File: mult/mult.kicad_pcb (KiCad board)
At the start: 2 copper layers, 76 parts, among them J1 Eurorack_Power, J10 Eurorack_Mono_Jack, J11 Eurorack_Mono_Jack, J12 Eurorack_Mono_Jack, J13 Eurorack_Mono_Jack, J14 Eurorack_Mono_Jack, J15 Eurorack_Mono_Jack, J16 Eurorack_Mono_Jack, J17 Eurorack_Mono_Jack, J2 Eurorack_Mono_Jack, J3 Eurorack_Mono_Jack, J4 Eurorack_Mono_Jack, J5 Eurorack_Mono_Jack, J6 Eurorack_Mono_Jack, J7 Eurorack_Mono_Jack, J8 Eurorack_Mono_Jack, J9 Eurorack_Mono_Jack, U1 OPA4197xPW, U2 OPA4197xPW, U3 OPA4197xPW, U4 OPA4197xPW, U5 LM324

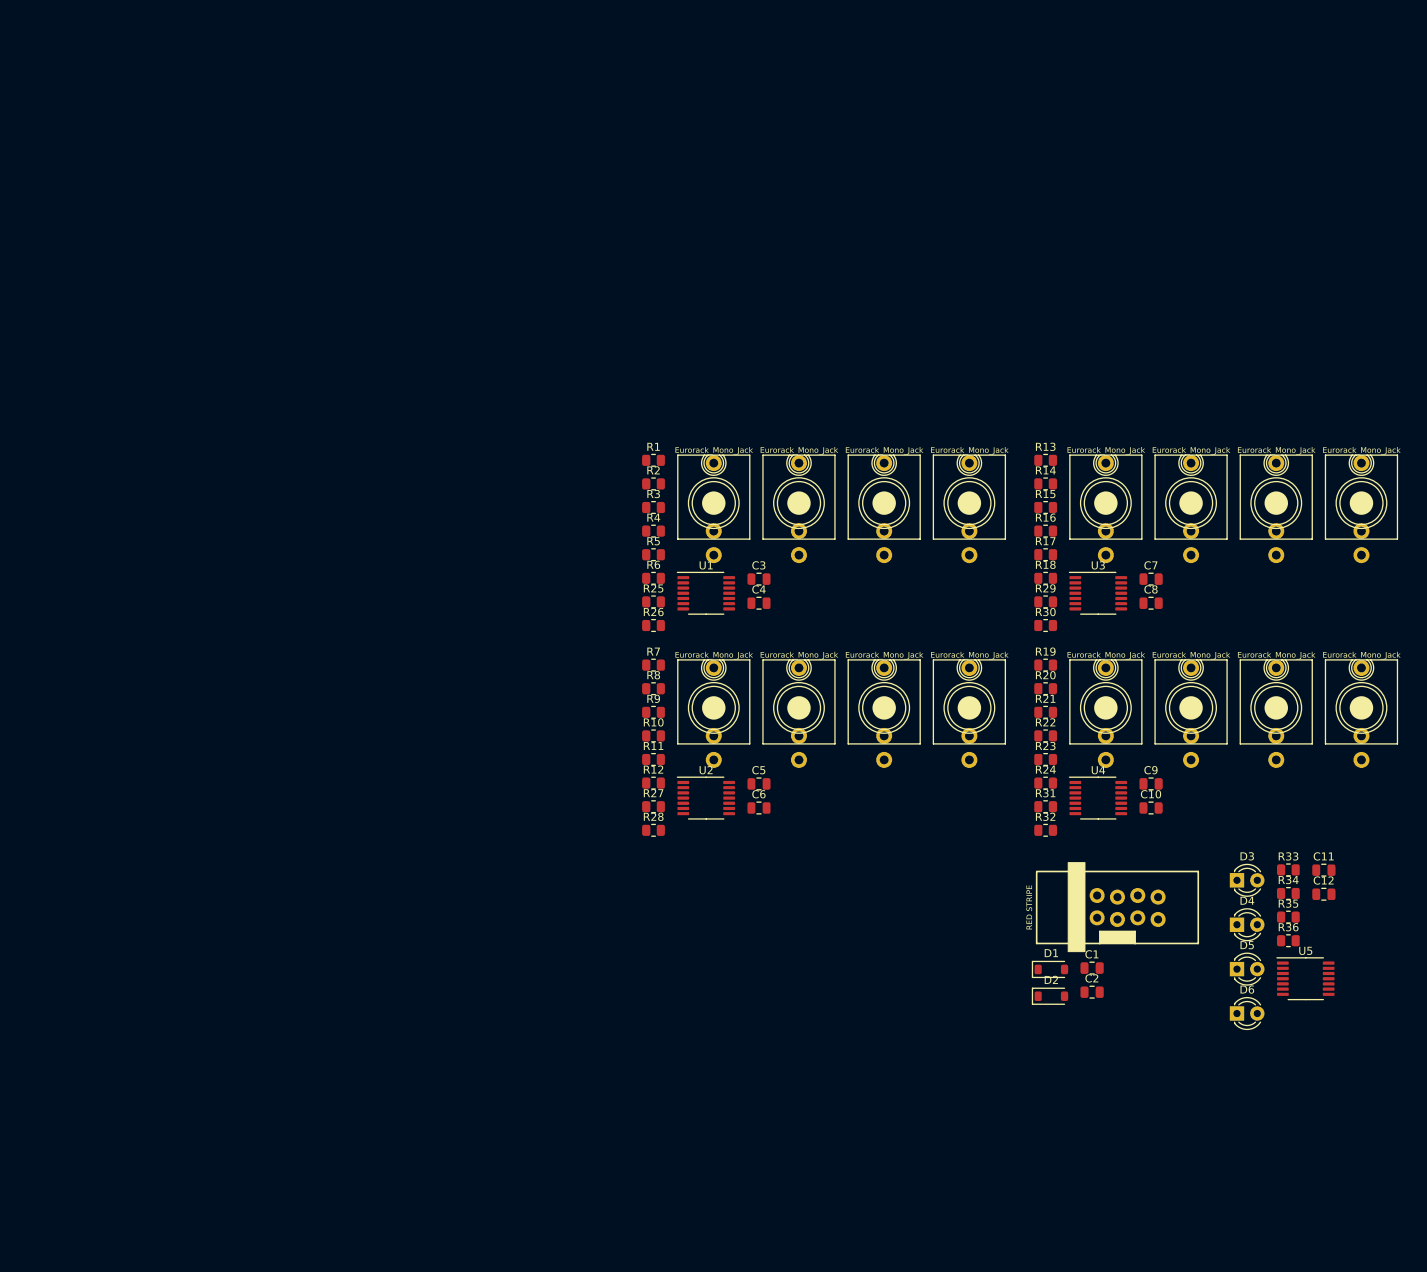
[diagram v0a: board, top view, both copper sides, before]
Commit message: mult: Misc partial progress
At least since last commit:

* New LEDs (no dual unit)
* Jack placement, share sleeve pin
* Board fit within 20x108mm
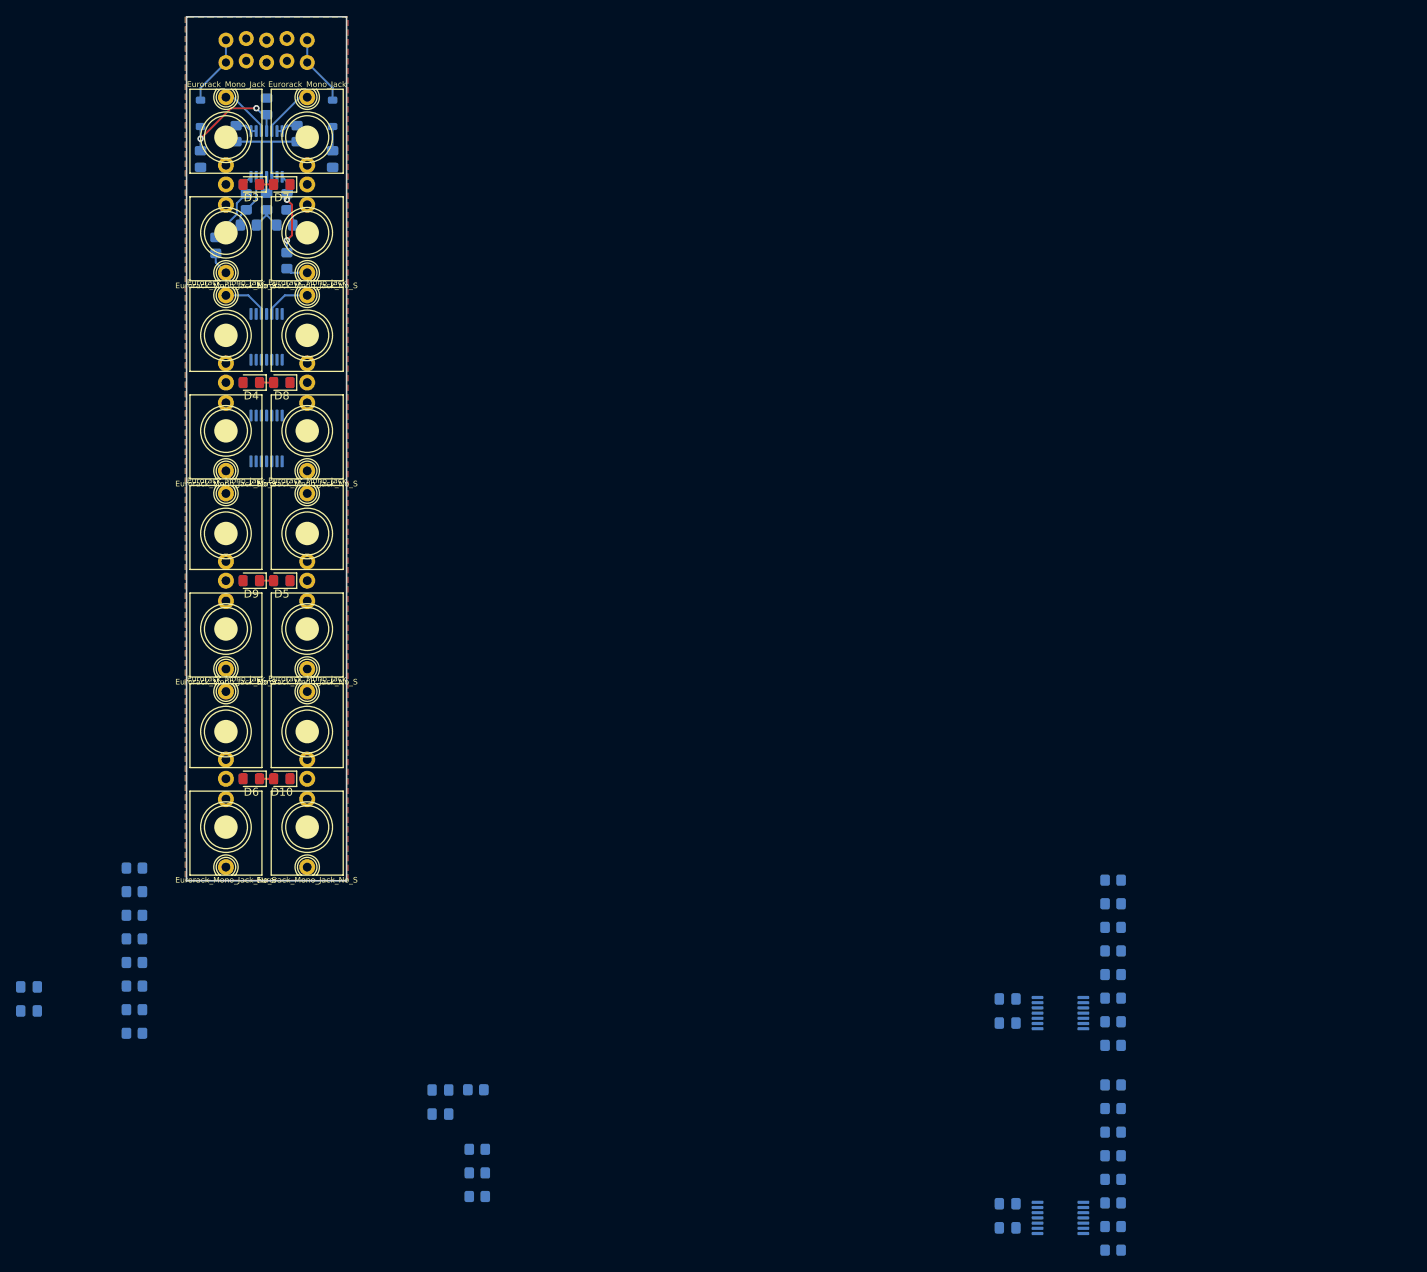
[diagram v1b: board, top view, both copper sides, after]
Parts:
- added D10: LED, LED_SMD:LED_0805_2012Metric_Pad1.15x1.40mm_HandSolder, F.Cu at (12.1, 95.2)
- added D7: LED, LED_SMD:LED_0805_2012Metric_Pad1.15x1.40mm_HandSolder, F.Cu at (12.1, 21.0)
- added D8: LED, LED_SMD:LED_0805_2012Metric_Pad1.15x1.40mm_HandSolder, F.Cu at (12.1, 45.7)
- added D9: LED, LED_SMD:LED_0805_2012Metric_Pad1.15x1.40mm_HandSolder, F.Cu at (8.26, 70.5)
- C1, C10, C11, C12, C2, C3, C4, C5, C6, C7, C8, C9: footprint Capacitor_SMD:C_0805_2012Metric -> Capacitor_SMD:C_0805_2012Metric_Pad1.18x1.45mm_HandSolder; moved to B.Cu
- D1, D2, J1, U1, U2, U3, U4, U5: moved to B.Cu
- D3, D4, D5, D6: value LED_Dual_Bidirectional -> LED; footprint LED_THT:LED_D3.0mm -> LED_SMD:LED_0805_2012Metric_Pad1.15x1.40mm_HandSolder
- J10, J11, J14, J15, J2, J3, J6, J7: footprint winterbloom:AudioJack_WQP518MA -> winterbloom:AudioJack_WQP518MA_Compact_S
- J12, J13, J16, J17, J4, J5, J8, J9: value Eurorack_Mono_Jack -> Eurorack_Mono_Jack_No_S; footprint winterbloom:AudioJack_WQP518MA -> winterbloom:AudioJack_WQP518MA_No_S
- R1, R10, R11, R12, R13, R14, R15, R16, R17, R18, R19, R2, R20, R21, R22, R23, R24, R25, R26, R27, R28, R29, R3, R30, R31, R32, R33, R34, R35, R36, R4, R5, R6, R7, R8, R9: footprint Resistor_SMD:R_0805_2012Metric -> Resistor_SMD:R_0805_2012Metric_Pad1.20x1.40mm_HandSolder; moved to B.Cu
- moved D1 150.9 mm to (1.91, 12.1), turned to 90 degrees
- moved D3 150.8 mm to (8.26, 21.0), turned to 180 degrees
- moved C1 150.5 mm to (1.91, 17.8), turned to -90 degrees
- moved U5 146.4 mm to (10.2, 52.7), turned to -90 degrees
- moved J1 144.0 mm to (15.2, 5.61), turned to 180 degrees
- moved D2 142.3 mm to (18.4, 12.1), turned to -90 degrees
- moved C2 140.9 mm to (18.4, 17.8), turned to -90 degrees
- moved D4 140.6 mm to (8.26, 45.7), turned to 180 degrees
- moved J13 132.7 mm to (15.2, 76.5), turned to 180 degrees
- moved J17 132.6 mm to (15.2, 101.3), turned to 180 degrees
- moved J12 132.2 mm to (5.08, 76.5), turned to 180 degrees
- moved J16 132.1 mm to (5.08, 101.3), turned to 180 degrees
- moved D5 128.9 mm to (12.1, 70.5), turned to 180 degrees
- moved D6 126.7 mm to (8.26, 95.2), turned to 180 degrees
- moved C11 113.8 mm to (31.9, 134.2), turned to 180 degrees
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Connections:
- R3 pad 1: Net-(U1C--) -> Net-(U1D--)
- R4 pad 2: Net-(U1C--) -> Net-(U1D--)
- R5 pad 1: Net-(U1D--) -> Net-(U1C--)
- R6 pad 2: Net-(U1D--) -> Net-(U1C--)
- U1 pad 14: Net-(R26-Pad1) -> Net-(R25-Pad1)
- U1 pad 8: Net-(R25-Pad1) -> Net-(R26-Pad1)
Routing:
- net /channel 1/average(a,b): track 0.00 -> 16.4 mm
- net VCC: track 0.00 -> 14.1 mm, vias 0 -> 2
- net Net-(R26-Pad1): track 0.00 -> 9.78 mm, vias 0 -> 2
- net Net-(R25-Pad1): track 0.00 -> 9.12 mm
- net Net-(D2-K): track 0.00 -> 8.81 mm
- net Net-(D1-A): track 0.00 -> 8.81 mm
- net Net-(U1D--): track 0.00 -> 6.84 mm
- net Net-(J3-Tip): track 0.00 -> 6.58 mm
- net /channel 1/tip in (a): track 0.00 -> 6.58 mm
- net Net-(J7-Tip): track 0.00 -> 5.80 mm
- net /channel 2/tip in (a): track 0.00 -> 5.80 mm
- net VEE: track 0.00 -> 4.44 mm
- net GND: track 0.00 -> 4.23 mm
- net Net-(J4-Tip): track 0.00 -> 2.95 mm
- net Net-(U1B--): track 0.00 -> 2.79 mm
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- added copper zone on B.Cu, net GND
- added copper zone on F.Cu, net GND
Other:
- board outline added: 20 x 108 mm

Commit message: mult: Replicate all channel PCB layouts
To do this the Replicate Layout plugin was heavily used. Post-replicate
moved channel 2's op amp to leave room for the LED op-amp.

Starting to layout some LED capacitors and route power.
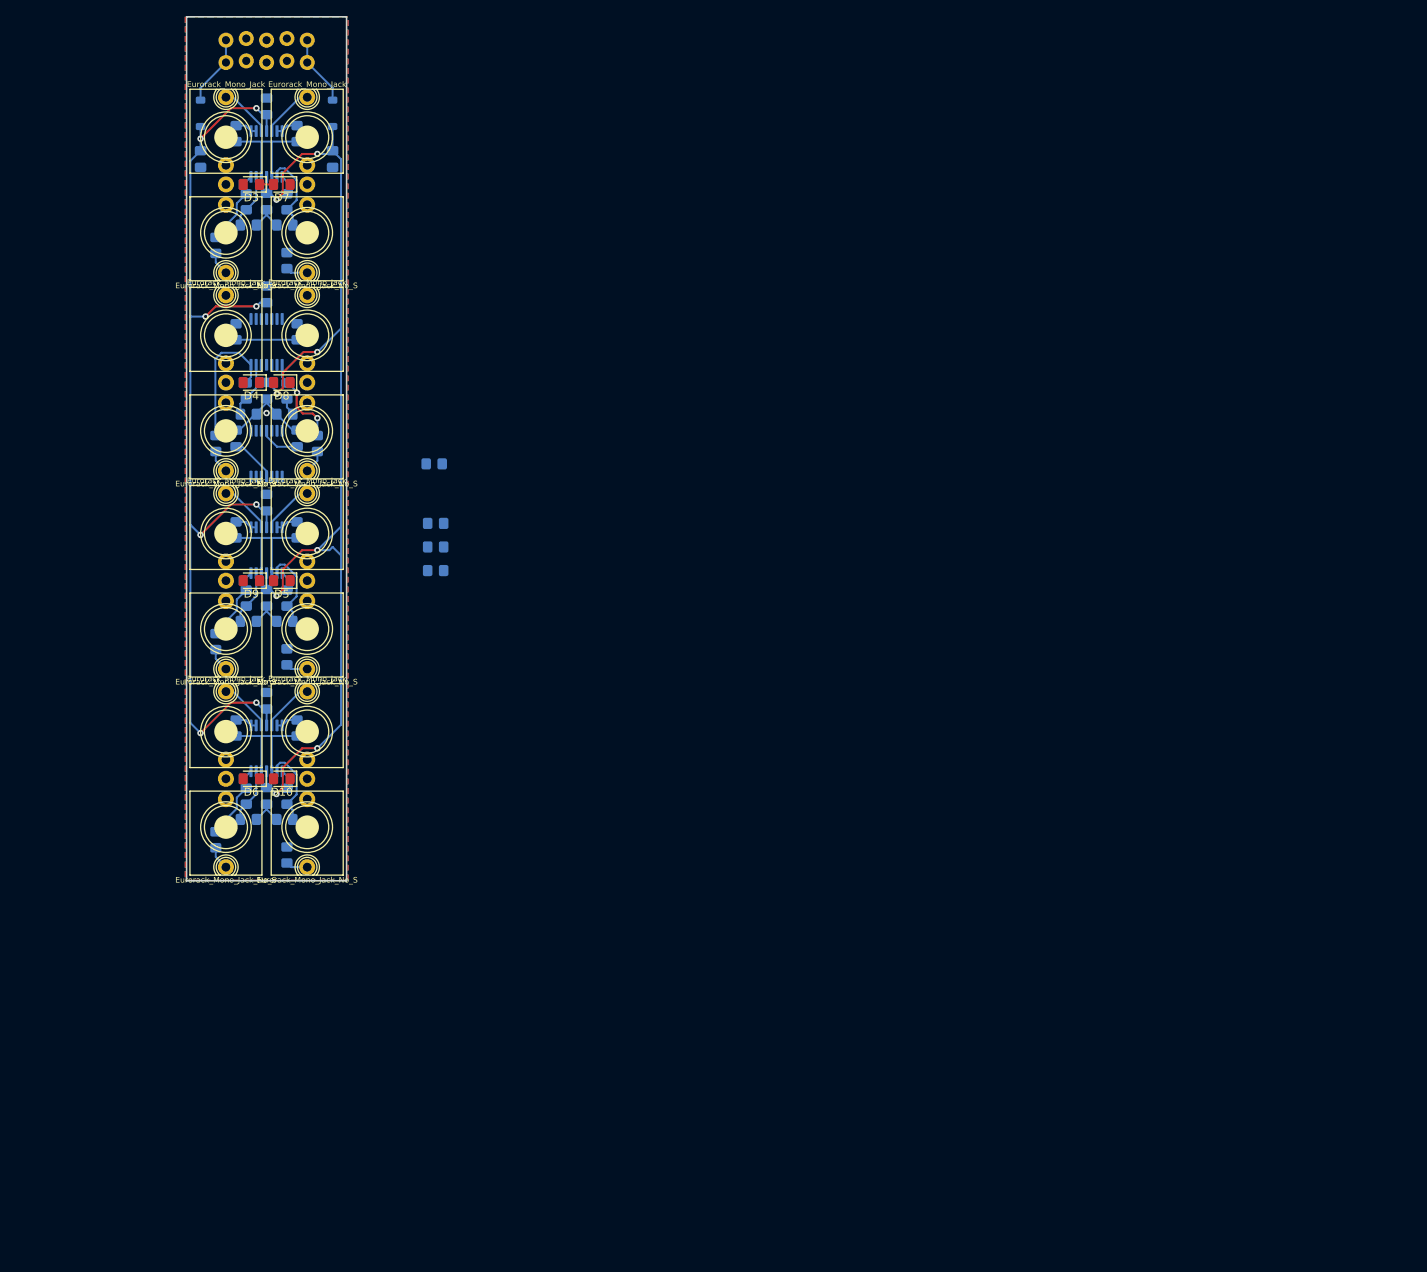
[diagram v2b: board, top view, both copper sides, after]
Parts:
- moved R31 122.1 mm to (3.81, 102.9), turned to -90 degrees
- moved R29 121.8 mm to (3.81, 78.1), turned to -90 degrees
- moved R19 118.4 mm to (6.35, 88.9), turned to -90 degrees
- moved R13 118.0 mm to (6.35, 64.1), turned to -90 degrees
- moved R21 116.2 mm to (7.62, 97.4), turned to 90 degrees
- moved R22 116.0 mm to (7.89, 100.3)
- moved R15 115.9 mm to (7.62, 72.7), turned to 90 degrees
- moved R16 115.7 mm to (7.89, 75.6)
- moved U4 115.3 mm to (10.2, 91.4), turned to -90 degrees
- moved U3 114.9 mm to (10.2, 66.7), turned to -90 degrees
- moved R32 114.5 mm to (12.7, 104.8), turned to -90 degrees
- moved R30 114.1 mm to (12.7, 80.0), turned to -90 degrees
- moved R24 114.1 mm to (12.4, 100.3), turned to 0 degrees
- moved R23 113.8 mm to (12.7, 97.4), turned to 90 degrees
- moved R18 113.8 mm to (12.4, 75.6), turned to 0 degrees
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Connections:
- R10 pad 2: Net-(U2C--) -> Net-(U2D--)
- R11 pad 1: Net-(U2D--) -> Net-(U2C--)
- R12 pad 2: Net-(U2D--) -> Net-(U2C--)
- R15 pad 1: Net-(U3C--) -> Net-(U3D--)
- R16 pad 2: Net-(U3C--) -> Net-(U3D--)
- R17 pad 1: Net-(U3D--) -> Net-(U3C--)
- R18 pad 2: Net-(U3D--) -> Net-(U3C--)
- R21 pad 1: Net-(U4C--) -> Net-(U4D--)
- R22 pad 2: Net-(U4C--) -> Net-(U4D--)
- R23 pad 1: Net-(U4D--) -> Net-(U4C--)
- R24 pad 2: Net-(U4D--) -> Net-(U4C--)
- R9 pad 1: Net-(U2C--) -> Net-(U2D--)
- U2 pad 14: Net-(R11-Pad2) -> Net-(R27-Pad1)
- U2 pad 8: Net-(R27-Pad1) -> Net-(R11-Pad2)
- U3 pad 14: Net-(R17-Pad2) -> Net-(R15-Pad2)
- U3 pad 8: Net-(R15-Pad2) -> Net-(R17-Pad2)
- U4 pad 14: Net-(R23-Pad2) -> Net-(R21-Pad2)
- U4 pad 8: Net-(R21-Pad2) -> Net-(R23-Pad2)
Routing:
- net VEE: track 4.44 -> 149.0 mm, vias 0 -> 8
- net VCC: track 14.1 -> 128.6 mm, vias 2 -> 8
- net GND: track 4.23 -> 23.6 mm, vias 0 -> 1
- net Net-(R27-Pad1): track 0.00 -> 17.4 mm
- net /channel 4/average(a,b): track 0.00 -> 16.4 mm
- net /channel 3/average(a,b): track 0.00 -> 16.4 mm
- net Net-(R11-Pad2): track 0.00 -> 11.4 mm, vias 0 -> 2
- net Net-(U3C--): track 0.00 -> 10.3 mm
- net Net-(U4C--): track 0.00 -> 10.3 mm
- net Net-(R21-Pad2): track 0.00 -> 9.12 mm
- net Net-(R15-Pad2): track 0.00 -> 9.12 mm
- net Net-(U1C--): track 2.21 -> 10.3 mm
- net /channel 2/average(a,b): track 0.00 -> 7.62 mm
- net Net-(R26-Pad1): track 9.78 -> 2.63 mm, vias 2 -> 0
- net Net-(U4D--): track 0.00 -> 6.84 mm
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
